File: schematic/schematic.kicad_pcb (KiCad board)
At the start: 4 copper layers, 0 parts

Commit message: Design PCB.
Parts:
- added 5v in: Conn_01x02, Connector_Wire:SolderWire-0.1sqmm_1x02_P3.6mm_D0.4mm_OD1mm, F.Cu at (131.4, 44.5)
- added C1: 68nF, Capacitor_SMD:C_0805_2012Metric_Pad1.18x1.45mm_HandSolder, F.Cu at (125.3, 86.9)
- added C2: 68nF, Capacitor_SMD:C_0805_2012Metric_Pad1.18x1.45mm_HandSolder, F.Cu at (129.0, 93.0)
- added C3: 68nF, Capacitor_SMD:C_0805_2012Metric_Pad1.18x1.45mm_HandSolder, F.Cu at (111.1, 105.8)
- added C4: 68nF, Capacitor_SMD:C_0805_2012Metric_Pad1.18x1.45mm_HandSolder, F.Cu at (111.3, 110.9)
- added GPIO: GPIO, TerminalBlock:TerminalBlock_Xinya_XY308-2.54-10P_1x10_P2.54mm_Horizontal, F.Cu at (121.5, 40.0)
- added IR rmt: LED, LED_THT:LED_D3.0mm_IRGrey, F.Cu at (52.0, 41.2)
- added R1: 10k, Resistor_SMD:R_0805_2012Metric_Pad1.20x1.40mm_HandSolder, F.Cu at (121.0, 88.0)
- added R2: 10k, Resistor_SMD:R_0805_2012Metric_Pad1.20x1.40mm_HandSolder, F.Cu at (123.2, 93.0)
- added R3: 10k, Resistor_SMD:R_0805_2012Metric_Pad1.20x1.40mm_HandSolder, F.Cu at (105.5, 106.8)
- added R4: 10k, Resistor_SMD:R_0805_2012Metric_Pad1.20x1.40mm_HandSolder, F.Cu at (105.5, 111.8)
- added R6: 10K, Resistor_SMD:R_0805_2012Metric_Pad1.20x1.40mm_HandSolder, F.Cu at (131.8, 50.5)
- added R7: 100R, Resistor_SMD:R_0805_2012Metric_Pad1.20x1.40mm_HandSolder, F.Cu at (53.0, 49.0)
- added REF**: MountingHole_2.5mm, MountingHole:MountingHole_2.5mm, F.Cu at (43.0, 119.0)
- added REF**: MountingHole_2.5mm, MountingHole:MountingHole_2.5mm, F.Cu at (43.0, 43.0)
- added REF**: MountingHole_2.5mm, MountingHole:MountingHole_2.5mm, F.Cu at (137.0, 43.0)
- added REF**: MountingHole_2.5mm, MountingHole:MountingHole_2.5mm, F.Cu at (137.0, 119.0)
- added U1: ESP32-S3-DevKitC, PCM_Espressif:ESP32-S3-DevKitC, F.Cu at (112.0, 92.8)
- added U2: pcm5122module, audio_boards:pcm5122_module, F.Cu at (70.1, 54.9)
- added audio out: Audio Out, TerminalBlock:TerminalBlock_Xinya_XY308-2.54-3P_1x03_P2.54mm_Horizontal, F.Cu at (46.0, 69.0)
- added oled128x64: ~, oled128x64_spi:oled128x64_spi, F.Cu at (62.0, 97.5)
- added station select: station select, rotary_encoder:XDCR_PEC11R-4220F-S0024, F.Cu at (125.5, 74.5)
- added volume: volume, rotary_encoder:XDCR_PEC11R-4220F-S0024, F.Cu at (126.5, 109.3)
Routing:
- net +3.3V: track 0.00 -> 163.4 mm, vias 0 -> 1
- net /ir_tx: track 0.00 -> 67.8 mm
- net /volume_sw: track 0.00 -> 63.7 mm
- net /spi_scl: track 0.00 -> 55.6 mm
- net /spi_mosi: track 0.00 -> 53.8 mm
- net /spi_res: track 0.00 -> 51.7 mm
- net /spi_dc: track 0.00 -> 50.0 mm
- net /spi_cs: track 0.00 -> 47.5 mm
- net Net-(U1-GPIO0): track 0.00 -> 47.0 mm, vias 0 -> 1
- net /lout: track 0.00 -> 43.9 mm
- net /GPIO41/MTDI: track 0.00 -> 43.7 mm
- net /GPIO40/MTDO: track 0.00 -> 42.9 mm
- net /rout: track 0.00 -> 41.5 mm
- net /i2c_sda: track 0.00 -> 35.7 mm
- net /i2c_scl: track 0.00 -> 35.7 mm
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- added copper zone on B.Cu, net GND
- added copper zone on F.Cu, net GND
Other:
- board outline added: 102 x 86 mm
- copper layers 4 -> 2
- board text added: "10"
- board text added: "100R"
- board text added: "10K"
- board text added: "11"
- board text added: "12"
- board text added: "13"
- board text added: "14"
- board text added: "2026-04-30"
- board text added: "3"
- board text added: "3v3"
- board text added: "40"
- board text added: "41"
- board text added: "5v"
- board text added: "68n"
- board text added: "9"
- board text added: "A"
- board text added: "B"
- board text added: "Internet Radio v3"
- board text added: "JLCJLCJLCJLC"
- board text added: "PCM5122"
- board text added: "agkeck"
- board text added: "gnd"
- board text added: "lout"
- board text added: "rout"

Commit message: Added minimal operating instructions to back silkscreen.
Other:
- board text added: "Connecting to wifi"
- board text added: "Station"
- board text added: "Volume"
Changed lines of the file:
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@@
 		(layer "F.SilkS")
+	)
+	(gr_circle
+		(center 125.55 74.45)
+		(end 128.95 74.55)
+		(stroke
+			(width 0.1524)
+			(type solid)
+		)
+		(fill yes)
+		(layer "B.SilkS")
+	)
+	(gr_circle
+		(center 126.55 108.9)
+		(end 129.95 109)
+		(stroke
+			(width 0.1524)
+			(type solid)
+		)
+		(fill yes)
+		(layer "B.SilkS")
 	)
 	(gr_line
@@
 			)
 			(justify left bottom)
+		)
+	)
+	(gr_text "Connecting to wifi"
+		(at 89.05 112.05 0)
+		(layer "B.SilkS")
+		(effects
+			(font
+				(size 1.524 1.524)
+				(thickness 0.3048)
+				(bold yes)
+			)
+			(justify left bottom mirror)
+		)
+	)
+	(gr_text "Volume"
+		(at 132.4 95.575 0)
+		(layer "B.SilkS")
+		(effects
+			(font
+				(size 1.524 1.524)
+				(thickness 0.3048)
+				(bold yes)
+			)
+			(justify left bottom mirror)
+		)
+	)
+	(gr_text "Station"
+		(at 132.55 85.45 0)
+		(layer "B.SilkS")
+		(effects
+			(font
+				(size 1.524 1.524)
+				(thickness 0.3048)
+				(bold yes)
+			)
+			(justify left bottom mirror)
+		)
+	)
+	(gr_text_box "Hold down volume button during reboot.  When the provisioning message {dblquote}Setup WIFI with ESP BLE Prov app{dblquote} shows on the screen use the app to supply wifi credentials."
+		(start 56.05 112.7)
+		(end 89.15 118.75)
+		(margins 1.0025 1.0025 1.0025 1.0025)
+		(layer "B.SilkS")
+		(effects
+			(font
+				(size 0.8128 0.8128)
+				(thickness 0.1016)
+			)
+			(justify left mirror)
+		)
+		(border yes)
+		(stroke
+			(width 0.1524)
+			(type solid)
+		)
+	)
+	(gr_text_box "rotate: adjust volume\nsingle press: toggle mute\ndouble press: toggle ir remote on/off"
+		(start 106.7 96.225)
+		(end 132.5 101.075)
+		(margins 1.0025 1.0025 1.0025 1.0025)
+		(layer "B.SilkS")
+		(effects
+			(font
+				(size 0.8128 0.8128)
+				(thickness 0.1016)
+			)
+			(justify left mirror)
+		)
+		(border yes)
+		(stroke
+			(width 0.1524)
+			(type solid)
+		)
+	)
+	(gr_text_box "rotate: scroll stations\nsingle press: show ip\nlong press: reboot"
+		(start 116.35 86.2)
+		(end 132.5 90.65)
+		(margins 1.0025 1.0025 1.0025 1.0025)
+		(layer "B.SilkS")
+		(effects
+			(font
+				(size 0.8128 0.8128)
+				(thickness 0.1016)
+			)
+			(justify left mirror)
+		)
+		(border yes)
+		(stroke
+			(width 0.1524)
+			(type solid)
 		)
 	)
@@
 		)
 	)
+	(group ""
+		(members "7fe73e01-3063-4cd3-baa4-eaf26c5ca502" "8d41e40b-8078-461a-8756-547e51655892")
+	)
+	(group ""
+		(members "894c9a0b-e514-4537-a5c1-8f373d67da75" "bcfb3d78-38b4-4422-8a3d-5a1829abdb4a")
+	)
+	(group ""
+		(members "a055911b-94da-4c25-9d7a-090fd3cf1ab4" "df499d2e-b343-461b-bfb8-932196944a43")
+	)
 	(embedded_fonts no)

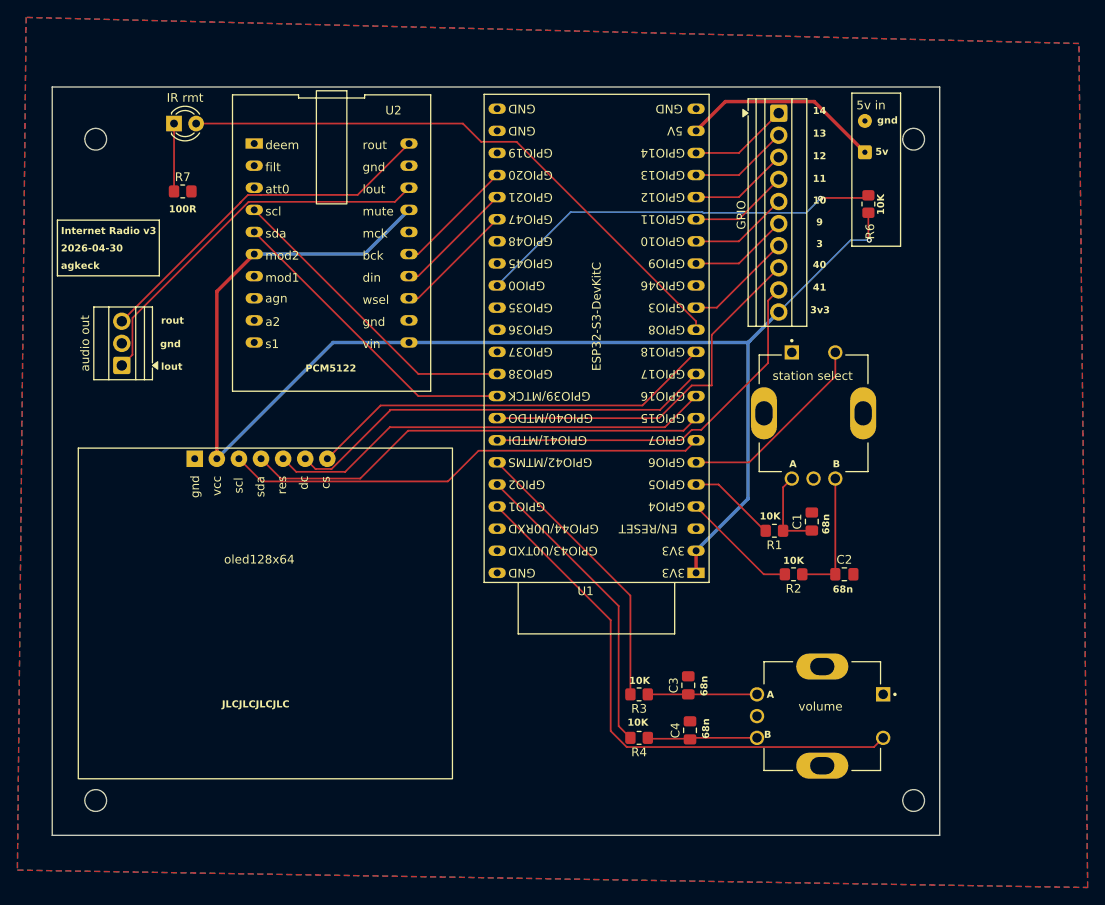
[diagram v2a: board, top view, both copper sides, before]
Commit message: Reassigned volume encoder pins in order to reroute outside of the esp32 antenna.  Also added a keep out zone on both top and bottom around the antenna.
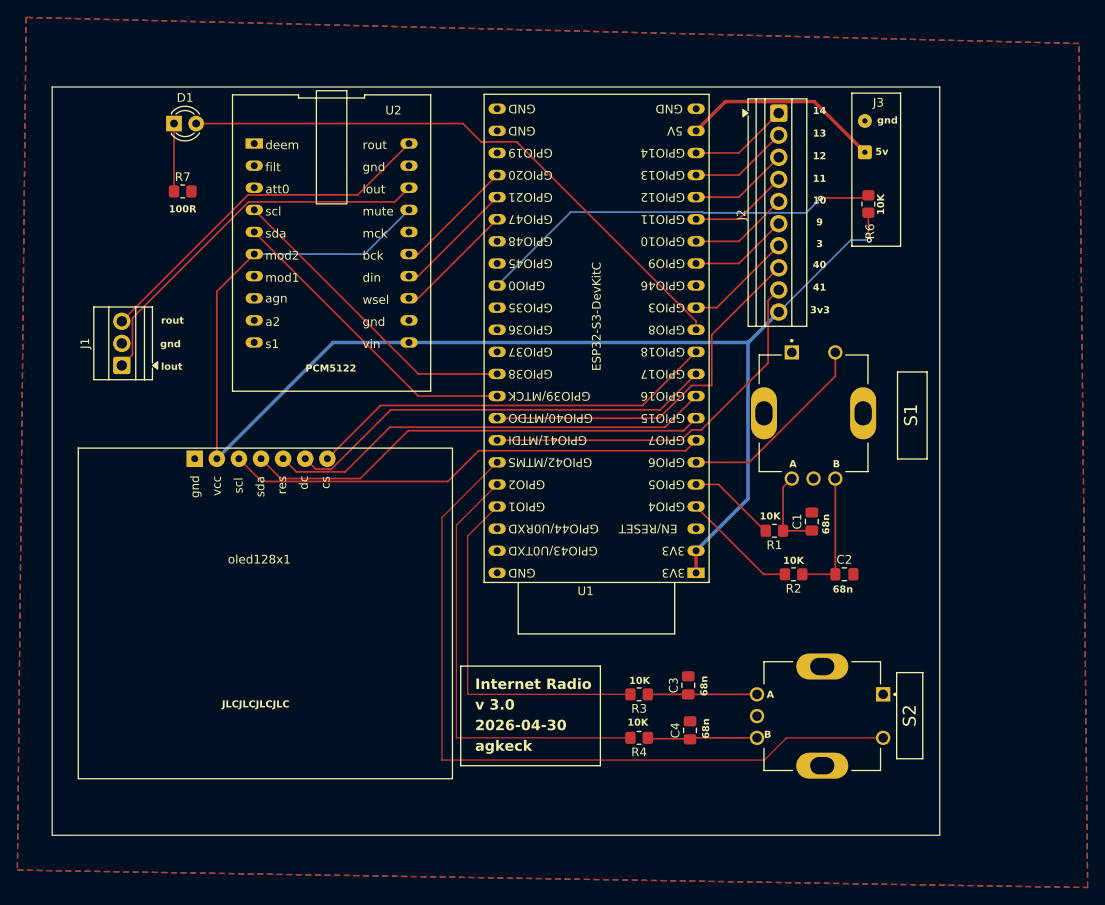
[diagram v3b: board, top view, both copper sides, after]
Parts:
- removed REF** (x4): MountingHole_2.5mm, MountingHole:MountingHole_2.5mm
- D1: renamed from IR rmt
- J1: renamed from audio out
- J3: renamed from 5v in
- S1: renamed from station select; value station select -> PEC11R-4220F-S0024
- S2: renamed from volume; value volume -> PEC11R-4220F-S0024
- renumbered GPIO to J2, oled128x64 to oled128x1
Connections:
- U1 pad 39: /volume_A -> /volume_sw
- U1 pad 41: /volume_sw -> /volume_A
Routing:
- net /volume_sw: track 63.7 -> 88.6 mm
- net /volume_B: track 35.5 -> 51.1 mm
- net /volume_A: track 33.0 -> 41.7 mm
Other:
- board text added: "Internet Radio"
- board text added: "v 3.0"
- board text removed: "Internet Radio v3"

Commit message: Expanded keep out zone around antenna.  Recommendations suggest 15mm.   I am able to keep the ground plane out but there are still three pads and traces in the keep out region.  These are related to the volume button so they might not cause problems in practice.
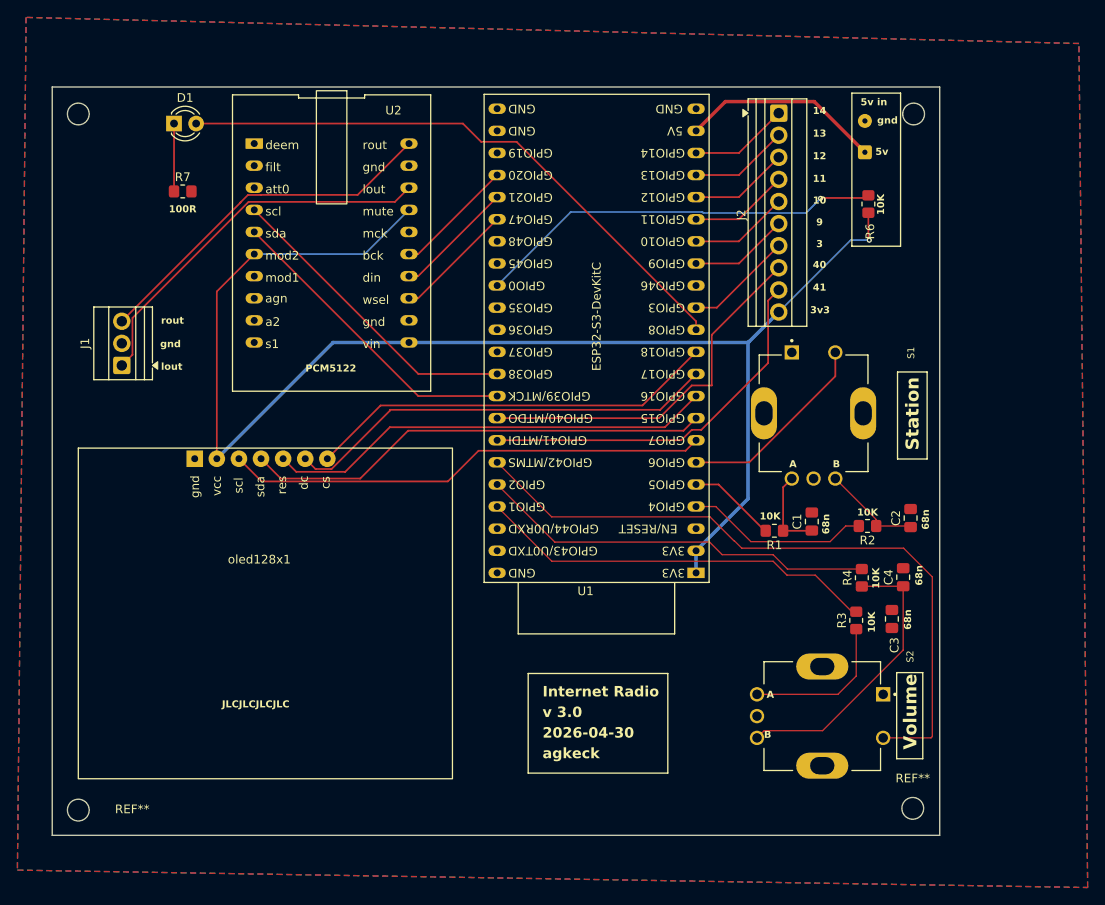
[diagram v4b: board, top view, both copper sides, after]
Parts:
- added REF**: MountingHole_2.5mm, MountingHole:MountingHole_2.5mm, F.Cu at (137.0, 40.1)
- added REF**: MountingHole_2.5mm, MountingHole:MountingHole_2.5mm, F.Cu at (41.0, 120.1)
- added REF**: MountingHole_2.5mm, MountingHole:MountingHole_2.5mm, F.Cu at (136.9, 119.9)
- added REF**: MountingHole_2.5mm, MountingHole:MountingHole_2.5mm, F.Cu at (41.0, 40.1)
- moved R4 31.5 mm to (131.1, 93.4), turned to 90 degrees
- moved C4 30.2 mm to (135.8, 93.3)
- moved R3 26.4 mm to (130.4, 98.3), turned to 90 degrees
- moved C3 24.6 mm to (134.5, 98.1)
- moved R2 10.2 mm to (131.7, 87.5)
- moved C2 9.99 mm to (136.7, 86.5), turned to 90 degrees
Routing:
- net Net-(C4-Pad1): track 12.8 -> 33.2 mm
- net /volume_sw: track 88.6 -> 79.5 mm
- net /station_B: track 13.4 -> 21.1 mm
- net /volume_B: track 51.1 -> 45.9 mm
- net Net-(C3-Pad1): track 12.5 -> 17.7 mm
- net /volume_A: track 41.7 -> 46.3 mm
- net Net-(C2-Pad1): track 14.8 -> 11.6 mm
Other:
- board text added: "5v in"

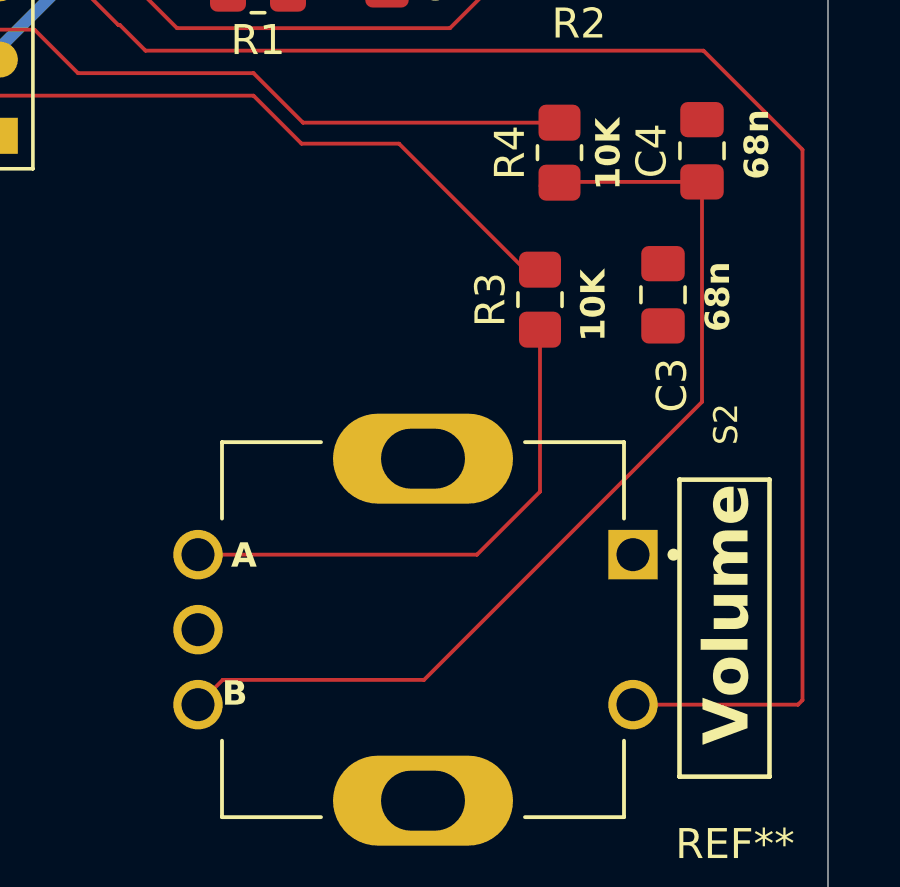
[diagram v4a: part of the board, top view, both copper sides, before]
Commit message: Added rounting for common on volume encoder.  The part of the volume encoder in the keep out region was the rotary encoder.  Without the ground plane the common was not connected so I added a trace to the ground for the switch.  This was not flagged by the design rule check.
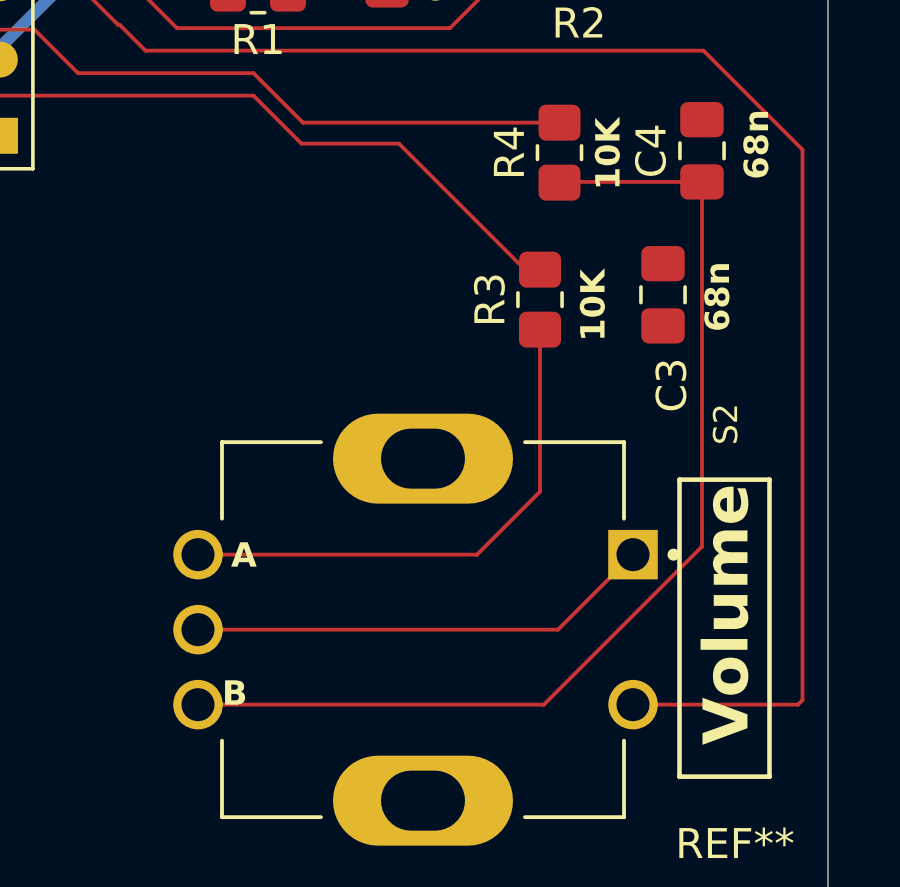
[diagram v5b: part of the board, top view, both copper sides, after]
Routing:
- net GND: track 0.00 -> 15.5 mm
- net Net-(C4-Pad1): track 33.2 -> 36.0 mm
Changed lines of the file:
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@@
+	)
+	(segment
+		(start 119 109.3)
+		(end 131 109.3)
+		(width 0.127)
+		(layer "F.Cu")
+		(net 1)
+	)
+	(segment
+		(start 131 109.3)
+		(end 133.5 106.8)
+		(width 0.127)
+		(layer "F.Cu")
+		(net 1)
 	)
 	(segment
@@
 	)
 	(segment
+		(start 135.8 106.531)
+		(end 135.8 94.375)
+		(width 0.127)
+		(layer "F.Cu")
+		(net 3)
+	)
+	(segment
 		(start 119 111.8)
-		(end 119.825 110.975)
+		(end 130.531 111.8)
 		(width 0.127)
 		(layer "F.Cu")
@@
 	)
 	(segment
-		(start 126.53421 110.975)
-		(end 135.8 101.70921)
-		(width 0.127)
-		(layer "F.Cu")
-		(net 3)
-	)
-	(segment
-		(start 135.8 101.70921)
-		(end 135.8 94.375)
-		(width 0.127)
-		(layer "F.Cu")
-		(net 3)
-	)
-	(segment
-		(start 119.825 110.975)
-		(end 126.53421 110.975)
+		(start 130.531 111.8)
+		(end 135.8 106.531)
 		(width 0.127)
 		(layer "F.Cu")
@@
 		(min_thickness 0.25)
 		(filled_areas_thickness no)
-		(fill yes
+		(fill
 			(thermal_gap 0.5)
 			(thermal_bridge_width 0.5)
